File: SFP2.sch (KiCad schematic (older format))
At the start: 19 parts, among them J6 1888247-1:TE_1888247-1

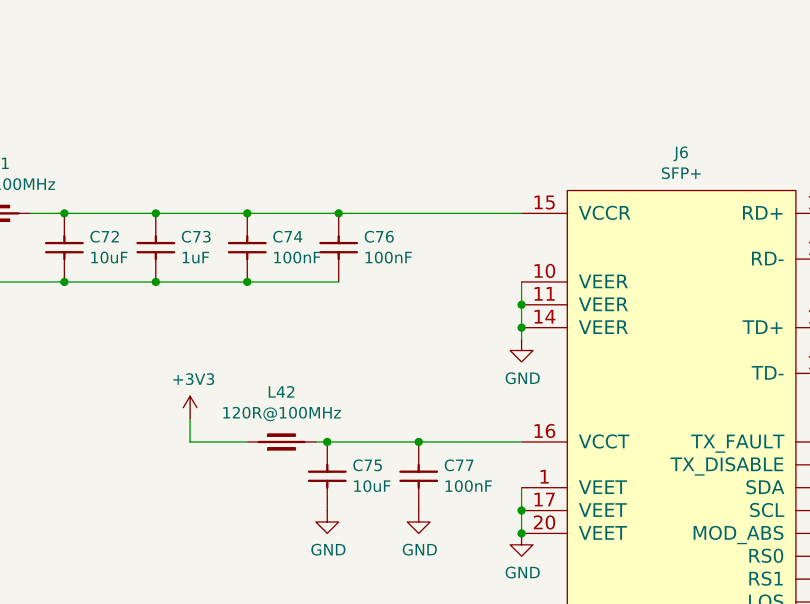
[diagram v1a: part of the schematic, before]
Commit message: SW2 placement changed, BOM cleared, FPGA boot, less ERC errors and wornings
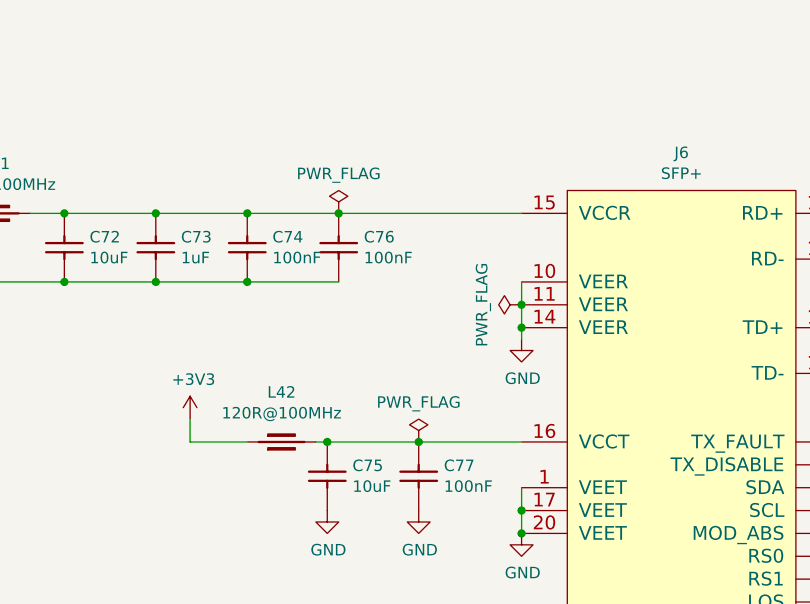
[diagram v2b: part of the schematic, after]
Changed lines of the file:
@@
 	6250 3550 6250 4000
 Connection ~ 4300 3350
+$Comp
+L power:PWR_FLAG #FLG?
+U 1 1 5D1DC2F9
+P 3850 2950
+AR Path="/5BABAC65/5D1DC2F9" Ref="#FLG?"  Part="1"
+AR Path="/5CC393D3/5D1DC2F9" Ref="#FLG0106"  Part="1"
+F 0 "#FLG0106" H 3850 3025 50  0001 C CNN
+F 1 "PWR_FLAG" H 3850 3123 50  0000 C CNN
+F 2 "" H 3850 2950 50  0001 C CNN
+F 3 "~" H 3850 2950 50  0001 C CNN
+	1    3850 2950
+	1    0    0    -1
+$EndComp
+$Comp
+L power:PWR_FLAG #FLG?
+U 1 1 5D1DDD1F
+P 3500 1950
+AR Path="/5BABAC65/5D1DDD1F" Ref="#FLG?"  Part="1"
+AR Path="/5CC393D3/5D1DDD1F" Ref="#FLG0107"  Part="1"
+F 0 "#FLG0107" H 3500 2025 50  0001 C CNN
+F 1 "PWR_FLAG" H 3500 2123 50  0000 C CNN
+F 2 "" H 3500 1950 50  0001 C CNN
+F 3 "~" H 3500 1950 50  0001 C CNN
+	1    3500 1950
+	1    0    0    -1
+$EndComp
+$Comp
+L power:PWR_FLAG #FLG?
+U 1 1 5D966080
+P 4300 2350
+AR Path="/5BABAC65/5D966080" Ref="#FLG?"  Part="1"
+AR Path="/5CC393D3/5D966080" Ref="#FLG0155"  Part="1"
+F 0 "#FLG0155" H 4300 2425 50  0001 C CNN
+F 1 "PWR_FLAG" H 4300 2523 50  0000 C CNN
+F 2 "" H 4300 2350 50  0001 C CNN
+F 3 "~" H 4300 2350 50  0001 C CNN
+	1    4300 2350
+	0    -1   -1   0
+$EndComp
 $EndSCHEMATC

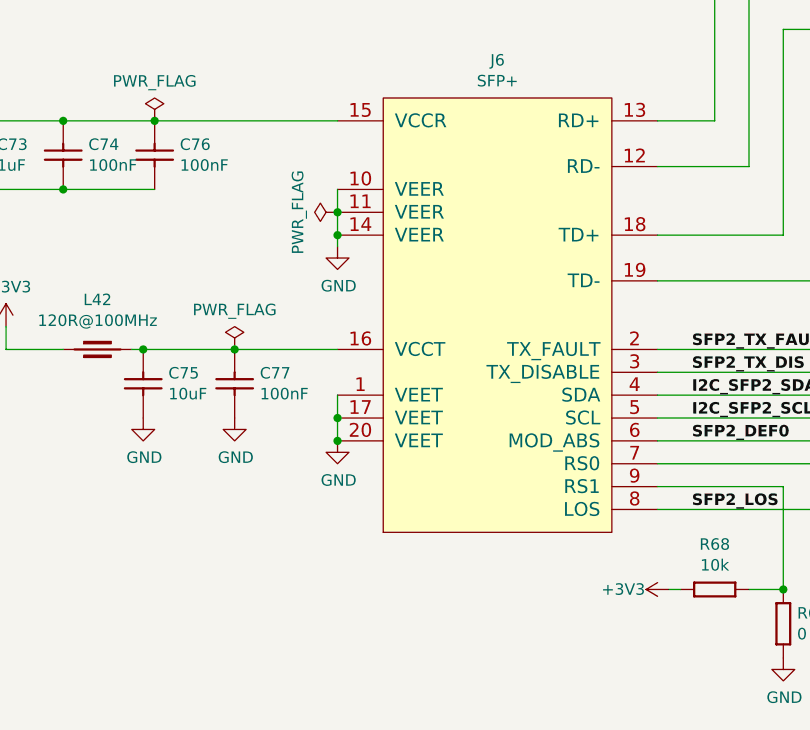
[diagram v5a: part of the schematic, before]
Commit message: SCH: shave down ERC to 1 error, 0 warning
  * 1 unavoidable error due to the unpopulated crystal Y2
  * change many pin types in symbol libraries (also for FMC con.)
  * as a result, could remove some power flags
  * fix footrint attribute for SFP module symbols

for most devices (not voltage regulators):
  * vcc = power input
  * gnd = power input
  * gpios (also FMC lanes) = bidirectional
  * configuration pins (tied to vcc / gnd) = inputs
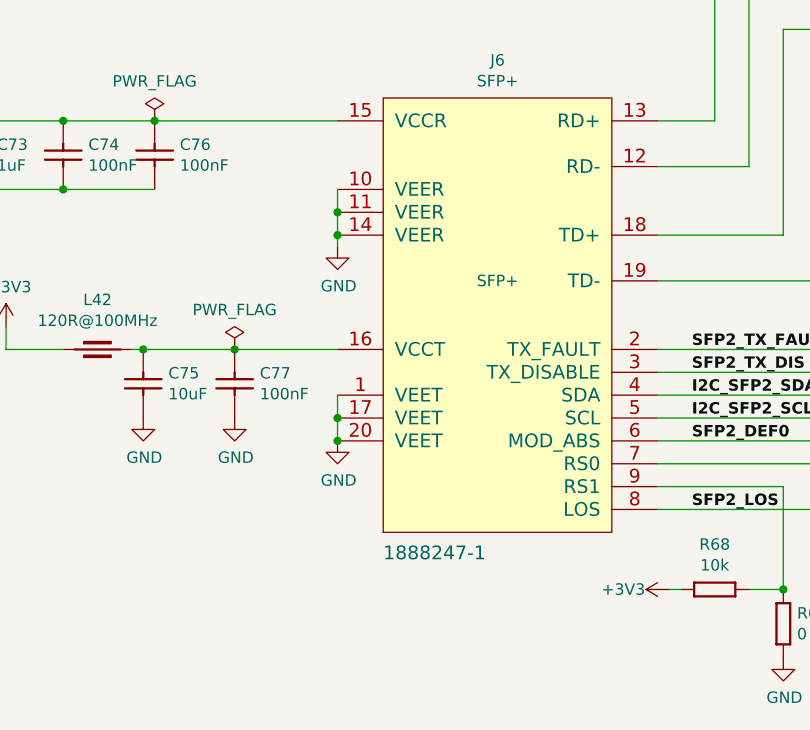
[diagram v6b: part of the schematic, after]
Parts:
- J6: value 1888247-1:TE_1888247-1 -> 1888247-1; footprint 1888247-1:TE_1888247-1 -> Marble:TE_1888247-1; Case ~~ -> (none); Comment ~~ -> (none); ComponentLink1Description ~~ -> (none); ComponentLink2Description ~~ -> (none); Database Table Name (none) -> TYCO; Device ~~ -> (none); Footprint Library (none) -> TYCO SMD; Library Name TYCO SMD -> Connectors.DbLib; PackageDescription ~~ -> (none); SCEM ~~ -> (none); Sense Comment ~~ -> (none); Status Comment ~~ -> (none)
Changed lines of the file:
@@
 AR Path="/5CC393D3/5C86C12C" Ref="J6"  Part="1"
 F 0 "J6" H 5000 2015 50  0000 C CNN
-F 1 "1888247-1:TE_1888247-1" H 4500 -140 60  0001 L CNN
-F 2 "1888247-1:TE_1888247-1" H 4500 -950 60  0001 L CNN
-F 3 "" H 4500 -320 60  0001 L CNN
+F 1 "1888247-1" H 4500 -140 60  0000 L CNN
+F 2 "Marble:TE_1888247-1" H 4500 -200 50  0001 L CNN
+F 3 "" H 4500 -275 50  0001 L CNN
 F 4 "SFP+" H 5000 1924 50  0000 C CNN "~"
-F 5 "TYCO_1888247-1" H 4500 -410 60  0001 L CNN "Part Number"
-F 6 "SFP+x1" H 4500 -500 60  0001 L CNN "Library Ref"
-F 7 "SchLib\\Connectors.SchLib" H 4500 -590 60  0001 L CNN "Library Path"
-F 8 "~~" H 4500 -680 60  0001 L CNN "Comment"
-F 9 "Standard" H 4500 -770 60  0001 L CNN "Component Kind"
-F 10 "Standard" H 4500 -860 60  0001 L CNN "Component Type"
-F 11 "~~" H 4500 -1040 60  0001 L CNN "PackageDescription"
-F 12 "20" H 4500 -1130 60  0001 L CNN "Pin Count"
-F 13 "~~" H 4500 -1220 60  0001 L CNN "Case"
-F 14 "PcbLib\\TYCO SMD.PcbLib" H 4500 -1310 60  0001 L CNN "Footprint Path"
-F 15 "TYCO_1888247-1" H 4500 -1400 60  0001 L CNN "Footprint Ref"
-F 16 "SFP+" H 4500 -1490 60  0001 L CNN "Family"
-F 17 "Yes" H 4500 -1580 60  0001 L CNN "Mounted"
-F 18 "No" H 4500 -1670 60  0001 L CNN "Socket"
-F 19 "Yes" H 4500 -1760 60  0001 L CNN "SMD"
-F 20 "No" H 4500 -1850 60  0001 L CNN "PressFit"
-F 21 "No" H 4500 -1940 60  0001 L CNN "Sense"
-F 22 "~~" H 4500 -2030 60  0001 L CNN "Sense Comment"
-F 23 "None" H 4500 -2120 60  0001 L CNN "Status"
-F 24 "~~" H 4500 -2210 60  0001 L CNN "Status Comment"
-F 25 "~~" H 4500 -2300 60  0001 L CNN "SCEM"
-F 26 "~~" H 4500 -2390 60  0001 L CNN "Device"
-F 27 "20 Position, Pitch 0.8mm SFP+ Receptacle (Small Form-factor Pluggable)" H 4500 -2480 60  0001 L CNN "Part Description"
-F 28 "TYCO ELECTRONICS" H 4500 -2570 60  0001 L CNN "Manufacturer"
-F 29 "1888247-1" H 4500 -2660 60  0001 L CNN "Manufacturer Part Number"
-F 30 "5.4mm" H 4500 -2750 60  0001 L CNN "ComponentHeight"
+F 5 "TYCO_1888247-1" H 4500 -350 50  0001 L CNN "Part Number"
+F 6 "SFP+x1" H 4500 -425 50  0001 L CNN "Library Ref"
+F 7 "SchLib\\Connectors.SchLib" H 4500 -500 50  0001 L CNN "Library Path"
+F 8 " " H 4500 -575 50  0001 L CNN "Comment"
+F 9 "Standard" H 4500 -650 50  0001 L CNN "Component Kind"
+F 10 "Standard" H 4500 -725 50  0001 L CNN "Component Type"
+F 11 " " H 4500 -800 50  0001 L CNN "PackageDescription"
+F 12 "20" H 4500 -875 50  0001 L CNN "Pin Count"
+F 13 " " H 4500 -950 50  0001 L CNN "Case"
+F 14 "PcbLib\\TYCO SMD.PcbLib" H 4500 -1025 50  0001 L CNN "Footprint Path"
+F 15 "TYCO_1888247-1" H 4500 -1100 50  0001 L CNN "Footprint Ref"
+F 16 "SFP+" H 5000 1050 50  0000 C CNN "Family"
+F 17 "Yes" H 4500 -1250 50  0001 L CNN "Mounted"
+F 18 "No" H 4500 -1325 50  0001 L CNN "Socket"
+F 19 "Yes" H 4500 -1400 50  0001 L CNN "SMD"
+F 20 "No" H 4500 -1475 50  0001 L CNN "PressFit"
+F 21 "No" H 4500 -1550 50  0001 L CNN "Sense"
+F 22 " " H 4500 -1625 50  0001 L CNN "Sense Comment"
+F 23 "None" H 4500 -1700 50  0001 L CNN "Status"
+F 24 " " H 4500 -1775 50  0001 L CNN "Status Comment"
+F 25 " " H 4500 -1850 50  0001 L CNN "SCEM"
+F 26 " " H 4500 -1925 50  0001 L CNN "Device"
+F 27 "20 Position, Pitch 0.8mm SFP+ Receptacle (Small Form-factor Pluggable)" H 4500 -2000 50  0001 L CNN "Part Description"
+F 28 "TYCO ELECTRONICS" H 4500 -2075 50  0001 L CNN "Manufacturer"
+F 29 "1888247-1" H 4500 -2150 50  0001 L CNN "Manufacturer Part Number"
+F 30 "5.4mm" H 4500 -2225 50  0001 L CNN "ComponentHeight"
 F 31 "~~" H 4500 -2840 60  0001 L CNN "ComponentLink1URL"
-F 32 "~~" H 4500 -2930 60  0001 L CNN "ComponentLink1Description"
+F 32 " " H 4500 -2300 50  0001 L CNN "ComponentLink1Description"
 F 33 "~~" H 4500 -3020 60  0001 L CNN "ComponentLink2URL"
-F 34 "~~" H 4500 -3110 60  0001 L CNN "ComponentLink2Description"
+F 34 " " H 4500 -2375 50  0001 L CNN "ComponentLink2Description"
 F 35 "\\\\cern.ch\\dfs\\Applications\\Altium\\Datasheets\\TYCO_1888247-1.pdf" H 4500 -3200 60  0001 L CNN "HelpURL"
-F 36 "CERN DEM JLC" H 4500 -3290 60  0001 L CNN "Author"
-F 37 "02/27/12 00:00:00" H 4500 -3380 60  0001 L CNN "CreateDate"
-F 38 "02/27/12 00:00:00" H 4500 -3470 60  0001 L CNN "LatestRevisionDate"
-F 39 "TYCO SMD" H 4500 -3560 60  0001 L CNN "Library Name"
-F 40 "This work is licensed under the Creative Commons CC-BY-SA 4.0 License. To the extent that circuit schematics that use Licensed Material can be considered to be ‘Adapted Material’, then the copyright holder waives article 3.b of the license with respect to these schematics." H 4500 -3650 60  0001 L CNN "License"
+F 36 "CERN DEM JLC" H 4500 -2450 50  0001 L CNN "Author"
+F 37 "02/27/12 00:00:00" H 4500 -2525 50  0001 L CNN "CreateDate"
+F 38 "02/27/12 00:00:00" H 4500 -2600 50  0001 L CNN "LatestRevisionDate"
+F 39 "Connectors.DbLib" H 4500 -2750 50  0001 L CNN "Library Name"
+F 40 "This work is licensed under the Creative Commons CC-BY-SA 4.0 License. To the extent that circuit schematics that use Licensed Material can be considered to be ‘Adapted Material’, then the copyright holder waives article 3.b of the license with respect to these schematics." H 4500 -2900 50  0001 L CNN "License"
+F 41 "TYCO" H 4500 -2675 50  0001 L CNN "Database Table Name"
+F 42 "TYCO SMD" H 4500 -2825 50  0001 L CNN "Footprint Library"
 	1    4500 1850
 	1    0    0    -1
@@
 	1    0    0    -1
 $EndComp
-$Comp
-L power:PWR_FLAG #FLG?
-U 1 1 5D966080
-P 4300 2350
-AR Path="/5BABAC65/5D966080" Ref="#FLG?"  Part="1"
-AR Path="/5CC393D3/5D966080" Ref="#FLG0155"  Part="1"
-F 0 "#FLG0155" H 4300 2425 50  0001 C CNN
-F 1 "PWR_FLAG" H 4300 2523 50  0000 C CNN
-F 2 "" H 4300 2350 50  0001 C CNN
-F 3 "~" H 4300 2350 50  0001 C CNN
-	1    4300 2350
-	0    -1   -1   0
-$EndComp
 $EndSCHEMATC

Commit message: Convert all footprints to use Marble nickname
Includes both .sch and .lib files
Includes both bare footprint names and those with CERN-like nicknames
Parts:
- C70, C74, C76, C77: footprint CAPC0603X33N -> Marble:CAPC0603X33N
- C71, C73: footprint CAPC1005X55N -> Marble:CAPC1005X55N
- C72, C75: footprint CAPC1608X87N -> Marble:CAPC1608X87N
- L41, L42: footprint INDC1608X65N -> Marble:INDC1608X65N
- R185, R68, R69, R70, R71, R72, R73, R74: footprint RESC1005X40N -> Marble:RESC1005X40N
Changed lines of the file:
@@
 F 0 "C70" V 1254 2060 50  0000 L CNN
 F 1 "CC0201_100NF_6.3V_10%_X5R" H 1150 1690 60  0001 L CNN
-F 2 "CAPC0603X33N" H 1150 880 60  0001 L CNN
+F 2 "Marble:CAPC0603X33N" H 1150 880 60  0001 L CNN
 F 3 "\\\\cern.ch\\dfs\\Applications\\Altium\\Datasheets\\CC0201_X5R_AVX.pdf" H 1150 1510 60  0001 L CNN
 F 4 "100nF" V 1345 2060 50  0000 L CNN "~"
@@
 F 0 "C74" V 3204 2060 50  0000 L CNN
 F 1 "CC0201_100NF_6.3V_10%_X5R" H 3100 1690 60  0001 L CNN
-F 2 "CAPC0603X33N" H 3100 880 60  0001 L CNN
+F 2 "Marble:CAPC0603X33N" H 3100 880 60  0001 L CNN
 F 3 "\\\\cern.ch\\dfs\\Applications\\Altium\\Datasheets\\CC0201_X5R_AVX.pdf" H 3100 1510 60  0001 L CNN
 F 4 "100nF" V 3295 2060 50  0000 L CNN "~"
@@
 F 0 "C76" V 3604 2060 50  0000 L CNN
 F 1 "CC0201_100NF_6.3V_10%_X5R" H 3500 1690 60  0001 L CNN
-F 2 "CAPC0603X33N" H 3500 880 60  0001 L CNN
+F 2 "Marble:CAPC0603X33N" H 3500 880 60  0001 L CNN
 F 3 "\\\\cern.ch\\dfs\\Applications\\Altium\\Datasheets\\CC0201_X5R_AVX.pdf" H 3500 1510 60  0001 L CNN
 F 4 "100nF" V 3695 2060 50  0000 L CNN "~"
@@
 F 0 "C77" V 3954 3060 50  0000 L CNN
 F 1 "CC0201_100NF_6.3V_10%_X5R" H 3850 2690 60  0001 L CNN
-F 2 "CAPC0603X33N" H 3850 1880 60  0001 L CNN
+F 2 "Marble:CAPC0603X33N" H 3850 1880 60  0001 L CNN
 F 3 "\\\\cern.ch\\dfs\\Applications\\Altium\\Datasheets\\CC0201_X5R_AVX.pdf" H 3850 2510 60  0001 L CNN
 F 4 "100nF" V 4045 3060 50  0000 L CNN "~"
@@
 F 0 "L41" H 2000 2167 50  0000 C CNN
 F 1 "IND0603_MURATA_BLM18SG121TN1D" H 1850 1760 60  0001 L CNN
-F 2 "INDC1608X65N" H 1850 950 60  0001 L CNN
+F 2 "Marble:INDC1608X65N" H 1850 950 60  0001 L CNN
 F 3 "\\\\cern.ch\\dfs\\Applications\\Altium\\Datasheets\\IND0603_MURATA_BLM18S.pdf" H 1850 1580 60  0001 L CNN
 F 4 "120R@100MHz" H 2000 2076 50  0000 C CNN "~"
@@
 F 0 "L42" H 3250 3167 50  0000 C CNN
 F 1 "IND0603_MURATA_BLM18SG121TN1D" H 3100 2760 60  0001 L CNN
-F 2 "INDC1608X65N" H 3100 1950 60  0001 L CNN
+F 2 "Marble:INDC1608X65N" H 3100 1950 60  0001 L CNN
 F 3 "\\\\cern.ch\\dfs\\Applications\\Altium\\Datasheets\\IND0603_MURATA_BLM18S.pdf" H 3100 2580 60  0001 L CNN
 F 4 "120R@100MHz" H 3250 3076 50  0000 C CNN "~"
@@
 F 0 "R70" V 6804 2710 50  0000 L CNN
 F 1 "R0402_10K_1%_0.0625W_100PPM" H 6700 2440 60  0001 L CNN
-F 2 "RESC1005X40N" H 6700 1630 60  0001 L CNN
+F 2 "Marble:RESC1005X40N" H 6700 1630 60  0001 L CNN
 F 3 "\\\\cern.ch\\dfs\\Applications\\Altium\\Datasheets\\R0402_Phycomp_RC0402.pdf" H 6700 2260 60  0001 L CNN
 F 4 "10k" V 6895 2710 50  0000 L CNN "~"
@@
 F 0 "R71" V 7054 2710 50  0000 L CNN
 F 1 "R0402_10K_1%_0.0625W_100PPM" H 6950 2440 60  0001 L CNN
-F 2 "RESC1005X40N" H 6950 1630 60  0001 L CNN
+F 2 "Marble:RESC1005X40N" H 6950 1630 60  0001 L CNN
 F 3 "\\\\cern.ch\\dfs\\Applications\\Altium\\Datasheets\\R0402_Phycomp_RC0402.pdf" H 6950 2260 60  0001 L CNN
 F 4 "10k" V 7145 2710 50  0000 L CNN "~"
@@
 F 0 "R72" V 7304 2710 50  0000 L CNN
 F 1 "R0402_10K_1%_0.0625W_100PPM" H 7200 2440 60  0001 L CNN
-F 2 "RESC1005X40N" H 7200 1630 60  0001 L CNN
+F 2 "Marble:RESC1005X40N" H 7200 1630 60  0001 L CNN
 F 3 "\\\\cern.ch\\dfs\\Applications\\Altium\\Datasheets\\R0402_Phycomp_RC0402.pdf" H 7200 2260 60  0001 L CNN
 F 4 "10k" V 7395 2710 50  0000 L CNN "~"
@@
 F 0 "R73" V 7554 2710 50  0000 L CNN
 F 1 "R0402_10K_1%_0.0625W_100PPM" H 7450 2440 60  0001 L CNN
-F 2 "RESC1005X40N" H 7450 1630 60  0001 L CNN
+F 2 "Marble:RESC1005X40N" H 7450 1630 60  0001 L CNN
 F 3 "\\\\cern.ch\\dfs\\Applications\\Altium\\Datasheets\\R0402_Phycomp_RC0402.pdf" H 7450 2260 60  0001 L CNN
 F 4 "10k" V 7645 2710 50  0000 L CNN "~"
@@
 F 0 "R74" V 7804 2710 50  0000 L CNN
 F 1 "R0402_10K_1%_0.0625W_100PPM" H 7700 2440 60  0001 L CNN
-F 2 "RESC1005X40N" H 7700 1630 60  0001 L CNN
+F 2 "Marble:RESC1005X40N" H 7700 1630 60  0001 L CNN
 F 3 "\\\\cern.ch\\dfs\\Applications\\Altium\\Datasheets\\R0402_Phycomp_RC0402.pdf" H 7700 2260 60  0001 L CNN
 F 4 "10k" V 7895 2710 50  0000 L CNN "~"
@@
 F 0 "R185" V 7854 3910 50  0000 L CNN
 F 1 "R0402_10K_1%_0.0625W_100PPM" H 7750 3640 60  0001 L CNN
-F 2 "RESC1005X40N" H 7750 2830 60  0001 L CNN
+F 2 "Marble:RESC1005X40N" H 7750 2830 60  0001 L CNN
 F 3 "\\\\cern.ch\\dfs\\Applications\\Altium\\Datasheets\\R0402_Phycomp_RC0402.pdf" H 7750 3460 60  0001 L CNN
 F 4 "10k" V 7945 3910 50  0000 L CNN "~"
@@
 F 0 "R68" H 6250 3803 50  0000 C CNN
 F 1 "R0402_10K_1%_0.0625W_100PPM" H 6100 3790 60  0001 L CNN
-F 2 "RESC1005X40N" H 6100 2980 60  0001 L CNN
+F 2 "Marble:RESC1005X40N" H 6100 2980 60  0001 L CNN
 F 3 "\\\\cern.ch\\dfs\\Applications\\Altium\\Datasheets\\R0402_Phycomp_RC0402.pdf" H 6100 3610 60  0001 L CNN
 F 4 "10k" H 6250 3894 50  0000 C CNN "~"
@@
 F 0 "R69" V 6354 4060 50  0000 L CNN
 F 1 "R0402_0R_JUMPER" H 6250 3790 60  0001 L CNN
-F 2 "RESC1005X40N" H 6250 2980 60  0001 L CNN
+F 2 "Marble:RESC1005X40N" H 6250 2980 60  0001 L CNN
 F 3 "\\\\cern.ch\\dfs\\Applications\\Altium\\Datasheets\\R0402_Phycomp_RC0402.pdf" H 6250 3610 60  0001 L CNN
 F 4 "0" V 6445 4060 50  0000 L CNN "~"
@@
 F 0 "C71" V 1704 2060 50  0000 L CNN
 F 1 "CC0402_1UF_16V_10%_X5R" H 1600 1690 60  0001 L CNN
-F 2 "CAPC1005X55N" H 1600 880 60  0001 L CNN
+F 2 "Marble:CAPC1005X55N" H 1600 880 60  0001 L CNN
 F 3 "\\\\cern.ch\\dfs\\Applications\\Altium\\Datasheets\\CC0402_X5R_TDK_C.pdf" H 1600 1510 60  0001 L CNN
 F 4 "1uF" V 1795 2060 50  0000 L CNN "~"
@@
 F 0 "C73" V 2804 2060 50  0000 L CNN
 F 1 "CC0402_1UF_16V_10%_X5R" H 2700 1690 60  0001 L CNN
-F 2 "CAPC1005X55N" H 2700 880 60  0001 L CNN
+F 2 "Marble:CAPC1005X55N" H 2700 880 60  0001 L CNN
 F 3 "\\\\cern.ch\\dfs\\Applications\\Altium\\Datasheets\\CC0402_X5R_TDK_C.pdf" H 2700 1510 60  0001 L CNN
 F 4 "1uF" V 2895 2060 50  0000 L CNN "~"
@@
 F 0 "C72" V 2496 2140 50  0000 R CNN
 F 1 "CC0603_10UF_6.3V_20%_X5R" H 2300 1990 60  0001 L CNN
-F 2 "CAPC1608X87N" H 2300 1180 60  0001 L CNN
+F 2 "Marble:CAPC1608X87N" H 2300 1180 60  0001 L CNN
 F 3 "\\\\cern.ch\\dfs\\Applications\\Altium\\Datasheets\\CC0603_X5R_KEMET.pdf" H 2300 1810 60  0001 L CNN
 F 4 "10uF" V 2405 2140 50  0000 R CNN "~"
@@
 F 0 "C75" V 3646 3140 50  0000 R CNN
 F 1 "CC0603_10UF_6.3V_20%_X5R" H 3450 2990 60  0001 L CNN
-F 2 "CAPC1608X87N" H 3450 2180 60  0001 L CNN
+F 2 "Marble:CAPC1608X87N" H 3450 2180 60  0001 L CNN
 F 3 "\\\\cern.ch\\dfs\\Applications\\Altium\\Datasheets\\CC0603_X5R_KEMET.pdf" H 3450 2810 60  0001 L CNN
 F 4 "10uF" V 3555 3140 50  0000 R CNN "~"
